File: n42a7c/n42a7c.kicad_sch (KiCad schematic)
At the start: 112 parts, among them J1 S2B-PH-SM4-TB, SW1 CPG151101S11-16, SW10 CPG151101S11-16, SW11 CPG151101S11-16, SW12 CPG151101S11-16, SW13 CPG151101S11-16, SW14 CPG151101S11-16, SW15 CPG151101S11-16, SW16 CPG151101S11-16, SW17 CPG151101S11-16, SW18 CPG151101S11-16, SW19 CPG151101S11-16, SW2 CPG151101S11-16, SW20 CPG151101S11-16, SW21 CPG151101S11-16, SW22 CPG151101S11-16, SW23 CPG151101S11-16, SW24 CPG151101S11-16, SW25 CPG151101S11-16, SW26 CPG151101S11-16, SW27 CPG151101S11-16, SW28 CPG151101S11-16, SW29 CPG151101S11-16, SW3 CPG151101S11-16, SW30 CPG151101S11-16, SW31 CPG151101S11-16, SW32 CPG151101S11-16, SW33 CPG151101S11-16, SW34 CPG151101S11-16, SW35 CPG151101S11-16, SW36 CPG151101S11-16, SW37 CPG151101S11-16, SW38 CPG151101S11-16, SW39 CPG151101S11-16, SW4 CPG151101S11-16, SW40 CPG151101S11-16, SW41 CPG151101S11-16, SW42 CPG151101S11-16, SW5 CPG151101S11-16, SW6 CPG151101S11-16, SW7 CPG151101S11-16, SW8 CPG151101S11-16, SW9 CPG151101S11-16, U1 XIAO-nRF52840-SMD

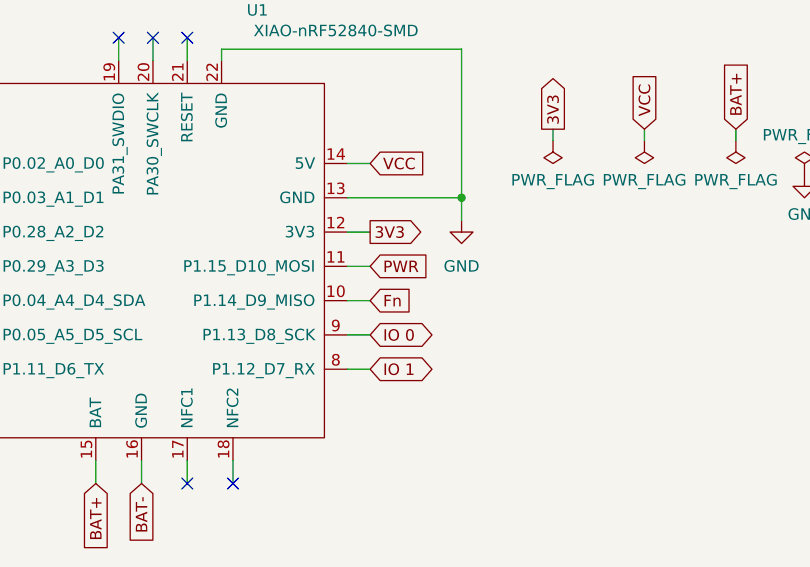
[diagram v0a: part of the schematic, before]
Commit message: correct foots
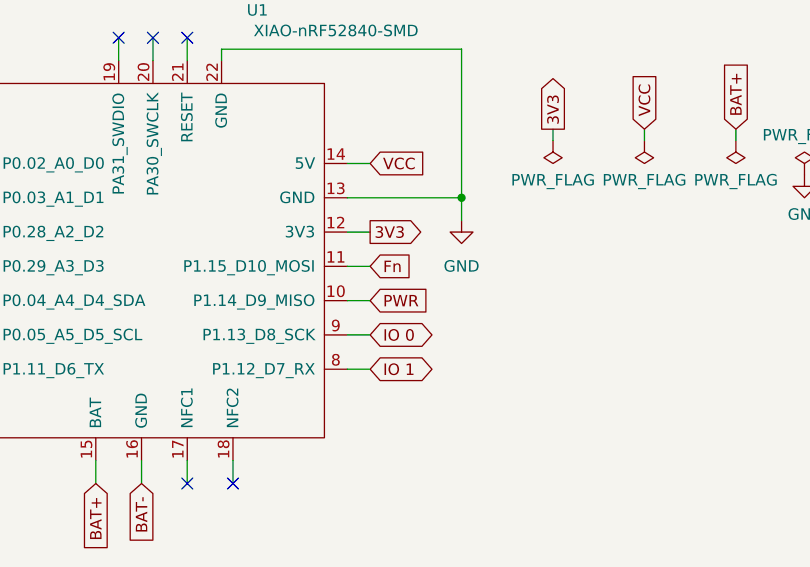
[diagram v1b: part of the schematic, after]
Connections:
- net Fn: now also U1.11 (P1.15_D10_MOSI); no longer U1.10 (P1.14_D9_MISO)
- net PWR: now also U1.10 (P1.14_D9_MISO); no longer U1.11 (P1.15_D10_MOSI)
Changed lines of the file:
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@@
 	(global_label "PWR"
 		(shape input)
-		(at 68.58 44.45 0)
-		(fields_autoplaced yes)
-		(effects
-			(font
-				(size 1.27 1.27)
-			)
-			(justify left)
-		)
-		(property "Intersheetrefs" "${INTERSHEET_REFS}"
-			(at 74.9024 44.45 0)
+		(at 68.58 48.26 0)
+		(fields_autoplaced yes)
+		(effects
+			(font
+				(size 1.27 1.27)
+			)
+			(justify left)
+		)
+		(property "Intersheetrefs" "${INTERSHEET_REFS}"
+			(at 74.9024 48.26 0)
 			(effects
 				(font
@@
 	(global_label "Fn"
 		(shape input)
-		(at 68.58 48.26 0)
-		(fields_autoplaced yes)
-		(effects
-			(font
-				(size 1.27 1.27)
-			)
-			(justify left)
-		)
-		(property "Intersheetrefs" "${INTERSHEET_REFS}"
-			(at 73.1486 48.26 0)
-			(effects
-				(font
+		(at 68.58 44.45 0)
+		(fields_autoplaced yes)
+		(effects
+			(font
+				(size 1.27 1.27)
+			)
+			(justify left)
+		)
+		(property "Intersheetrefs" "${INTERSHEET_REFS}"
+			(at 73.1486 44.45 0)
+			(effects
+				(font

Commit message: revise power conn
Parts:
- added J4: S2B-PH-SM4-TB, Connector_JST:JST_PH_S2B-PH-K_1x02_P2.00mm_Horizontal, symbol Connector_Generic:Conn_01x02
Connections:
- net BAT-: now also J4.2 (Pin_2)
- net at J1.1 (Pin_1), J2.1 (Pin_1), SW_HPWR1.C (B): now also J4.1 (Pin_1)
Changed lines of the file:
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@@
 	)
 	(junction
+		(at 63.5 168.91)
+		(diameter 0)
+		(color 0 0 0 0)
+	)
+	(junction
 		(at 237.49 95.25)
 		(diameter 0)
@@
 	)
 	(junction
+		(at 62.23 171.45)
+		(diameter 0)
+		(color 0 0 0 0)
+	)
+	(junction
 		(at 229.87 120.65)
 		(diameter 0)
@@
 	(wire
 		(pts
+			(xy 62.23 171.45) (xy 64.77 171.45)
+		)
+		(stroke
+			(width 0)
+			(type default)
+		)
+	)
+	(wire
+		(pts
 			(xy 219.71 85.09) (xy 219.71 95.25)
 		)
@@
 	(wire
 		(pts
+			(xy 63.5 168.91) (xy 64.77 168.91)
+		)
+		(stroke
+			(width 0)
+			(type default)
+		)
+	)
+	(wire
+		(pts
 			(xy 237.49 85.09) (xy 237.49 95.25)
 		)
@@
 					(unit 1)
 				)
+			)
+		)
+	)
+	(symbol
+		(lib_id "Connector_Generic:Conn_01x02")
+		(at 69.85 168.91 0)
+		(unit 1)
+		(exclude_from_sim no)
+		(in_bom yes)
+		(on_board yes)
+		(dnp no)
+		(property "Reference" "J4"
+			(at 69.85 166.37 0)
+			(effects
+				(font
+					(size 1.27 1.27)
+				)
+			)
+		)
+		(property "Value" "S2B-PH-SM4-TB"
+			(at 69.85 175.26 0)
+			(effects
+				(font
+					(size 1.27 1.27)
+				)
+				(hide yes)
+			)
+		)
+		(property "Footprint" "Connector_JST:JST_PH_S2B-PH-K_1x02_P2.00mm_Horizontal"
+			(at 69.85 168.91 0)
+			(effects
+				(font
+					(size 1.27 1.27)
+				)
+				(hide yes)
+			)
+		)
+		(property "Datasheet" "~"
+			(at 69.85 168.91 0)
+			(effects
+				(font
+					(size 1.27 1.27)
+				)
+				(hide yes)
+			)
+		)
+		(property "Description" "Generic connector, single row, 01x02, script generated (kicad-library-utils/schlib/autogen/connector/)"
+			(at 69.85 168.91 0)
+			(effects
+				(font
+					(size 1.27 1.27)
+				)
+				(hide yes)
+			)
+		)
+		(pin "2"
+		)
+		(pin "1"
+		)
+		(instances
+			(project "n42a7c"
+				(path "/c261125e-4de6-4ce6-97c8-cc9869147583"
+					(reference "J4")
+					(unit 1)
+				)

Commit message: revise switch
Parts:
- J2, J3: value ~ -> (none)
- renumbered SW_DR1 to SW_D1, SW_DR2 to SW_D2, SW_HPWR1 to SW_PWR1
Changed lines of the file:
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@@
 		(on_board yes)
 		(dnp no)
-		(property "Reference" "SW_DR1"
+		(property "Reference" "SW_D1"
 			(at 24.13 166.37 0)
 			(effects
@@
 			(project "n40a8c"
 				(path "/c261125e-4de6-4ce6-97c8-cc9869147583"
-					(reference "SW_DR1")
+					(reference "SW_D1")
 					(unit 1)
 				)
@@
 		(exclude_from_sim no)
 		(in_bom no)
-		(on_board no)
+		(on_board yes)
 		(dnp no)
 		(property "Reference" "J2"
@@
 			)
 		)
-		(property "Value" "~"
+		(property "Value" ""
 			(at 55.88 182.88 0)
 			(effects
@@
 		(on_board yes)
 		(dnp no)
-		(property "Reference" "SW_DR2"
+		(property "Reference" "SW_D2"
 			(at 43.18 166.37 0)
 			(effects
@@
 			(project "n42a7c"
 				(path "/c261125e-4de6-4ce6-97c8-cc9869147583"
-					(reference "SW_DR2")
+					(reference "SW_D2")
 					(unit 1)
 				)
@@
 		(exclude_from_sim no)
 		(in_bom no)
-		(on_board no)
+		(on_board yes)
 		(dnp no)
 		(property "Reference" "J3"
@@
 			)
 		)
-		(property "Value" "~"
+		(property "Value" ""
 			(at 55.88 190.5 0)
 			(effects
@@
 		(dnp no)
 		(fields_autoplaced yes)
-		(property "Reference" "SW_HPWR1"
+		(property "Reference" "SW_PWR1"
 			(at 80.01 170.18 0)
 			(effects
@@
 			(project ""
 				(path "/c261125e-4de6-4ce6-97c8-cc9869147583"
-					(reference "SW_HPWR1")
+					(reference "SW_PWR1")
 					(unit 1)
 				)

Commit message: revise
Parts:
- J2, J3: value (none) -> ~
- J4: value S2B-PH-SM4-TB -> S2B-PH-K
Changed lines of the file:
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@@
 			)
 		)
-		(property "Value" ""
+		(property "Value" "~"
 			(at 55.88 182.88 0)
 			(effects
@@
 			)
 		)
-		(property "Value" ""
+		(property "Value" "~"
 			(at 55.88 190.5 0)
 			(effects
@@
 			)
 		)
-		(property "Value" "S2B-PH-SM4-TB"
+		(property "Value" "S2B-PH-K"
 			(at 69.85 175.26 0)
 			(effects
